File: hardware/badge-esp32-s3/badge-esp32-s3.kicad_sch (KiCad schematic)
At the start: 1 part, among them J1 Connector, USB-TYPE-C-16P

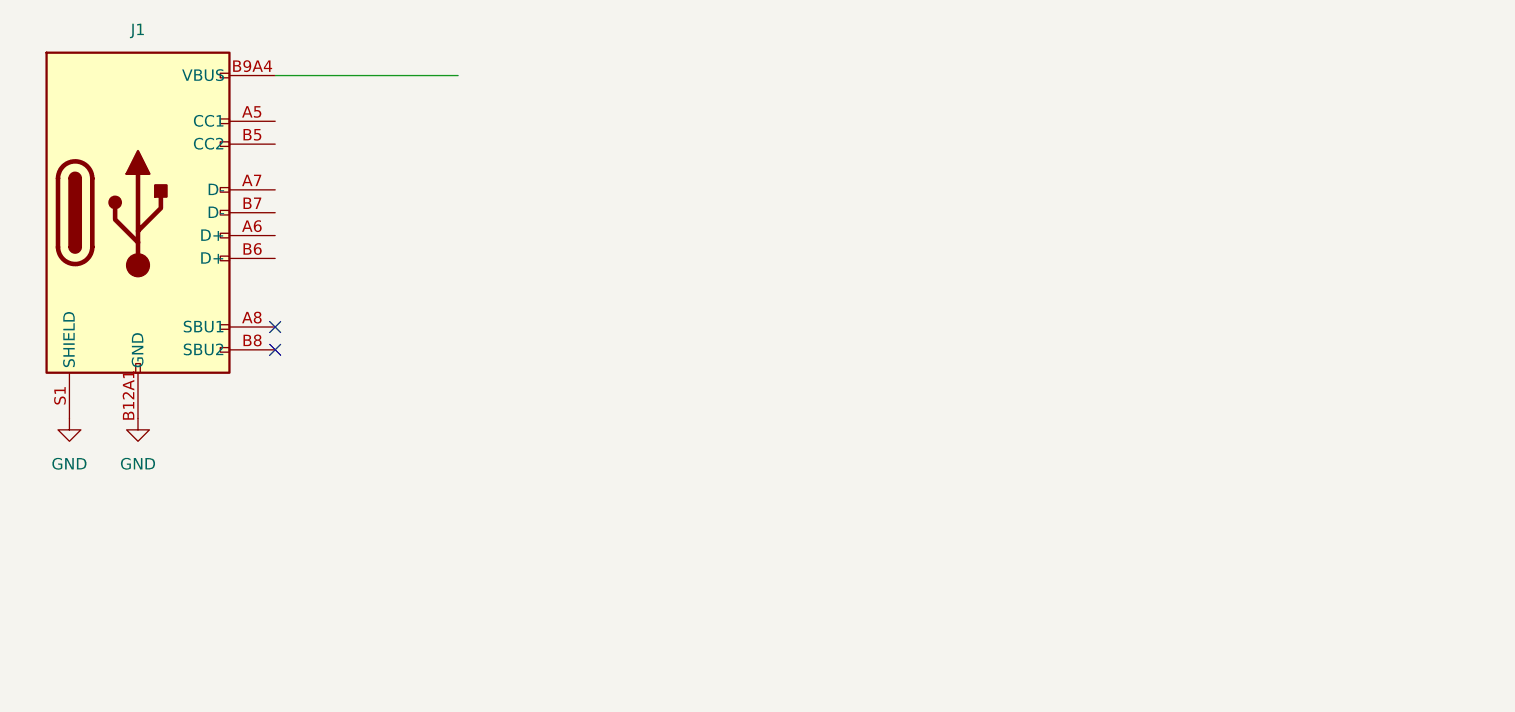
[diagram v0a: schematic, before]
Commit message: Finish USB sub-schematic
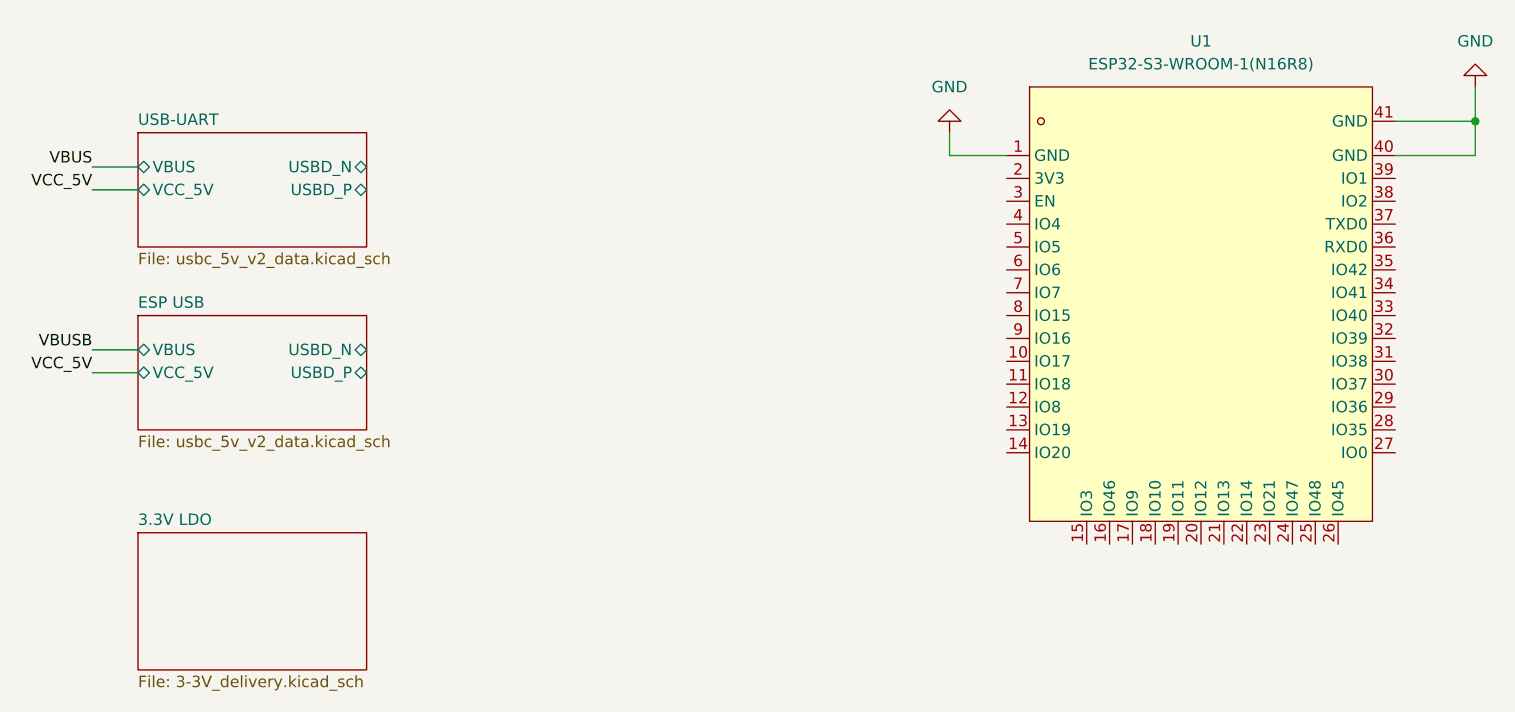
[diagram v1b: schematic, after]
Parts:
- removed J1: Connector, USB-TYPE-C-16P, PCM_JLCPCB:TYPE-C-SMD_HX-TYPE-C-16PIN, symbol PCM_JLCPCB-Extended:Connector, USB-TYPE-C-16P
- added U1: ESP32-S3-WROOM-1(N16R8), lcsc-lib:WIRELM-SMD_ESP32-S3-WROOM-1, symbol lcsc-lib:ESP32-S3-WROOM-1(N16R8)
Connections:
- net GND: now also U1.1 (GND), U1.40 (GND), U1.41 (GND)
- no-connect marks 2 -> 0
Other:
- added sheet 3.3V LDO (3-3V_delivery.kicad_sch)
- added sheet ESP USB (usbc_5v_v2_data.kicad_sch)
- added sheet USB-UART (usbc_5v_v2_data.kicad_sch)
